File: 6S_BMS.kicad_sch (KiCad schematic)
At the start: 46 parts, among them J1 JST_EH_B8B-EH-A, J2 BM06B-GHS-TBT, J3 Conn_ARM_SWD_TagConnect_TC203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, J5 Conn_01x04_Pin, J6 Conn_01x04_Pin, SW1 SW_SPST, U1 BQ76925RGER, U2 STM32L431KCUx, U5 TLV75533PDBV

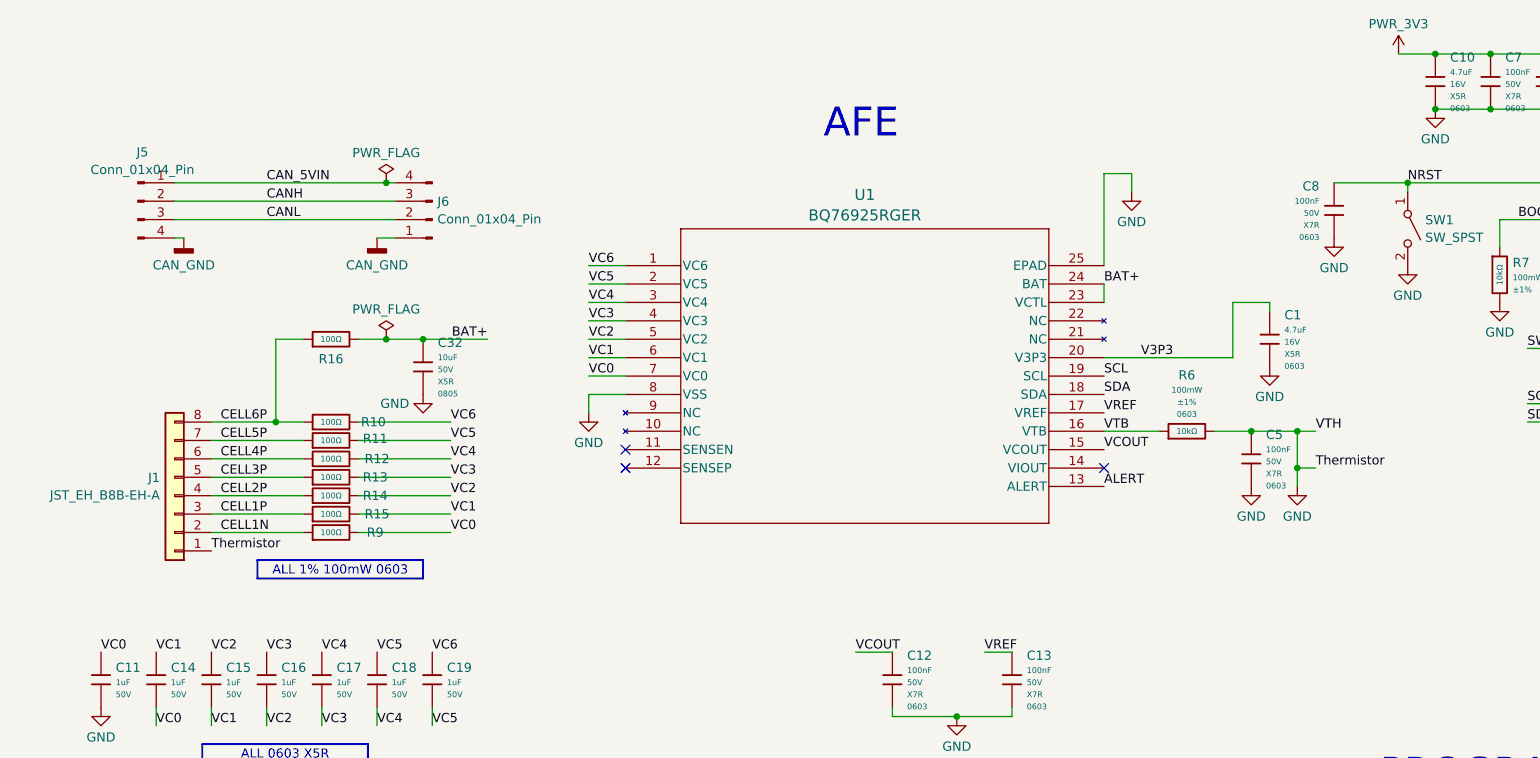
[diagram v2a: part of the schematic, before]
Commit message: Updated thermistor & layout
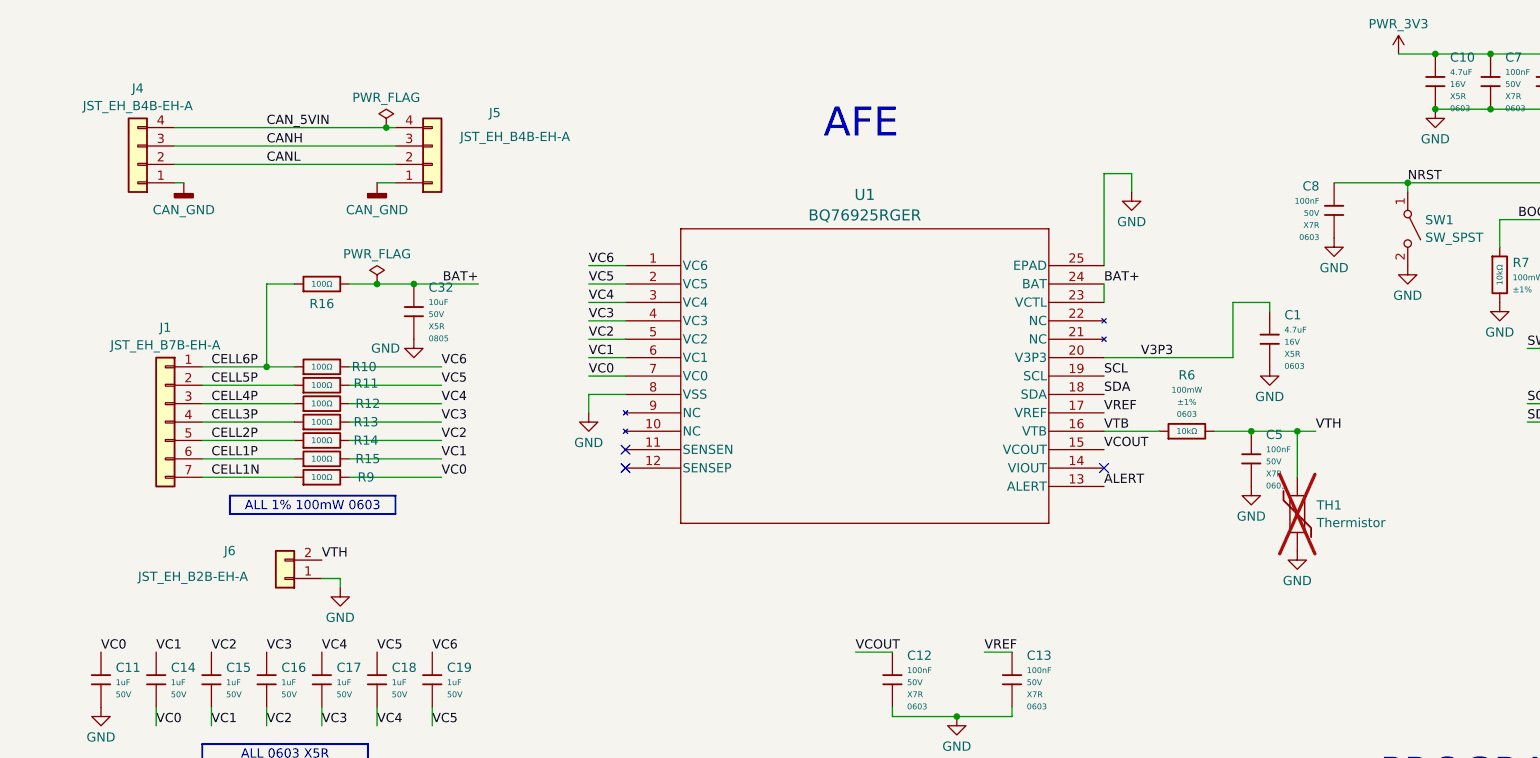
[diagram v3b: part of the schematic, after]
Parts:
- removed J1: JST_EH_B8B-EH-A, Connector_JST:JST_EH_B8B-EH-A_1x08_P2.50mm_Vertical, symbol Connector_Generic:Conn_01x08
- removed J5, J6: Conn_01x04_Pin, symbol Connector:Conn_01x04_Pin
- added J1: JST_EH_B7B-EH-A, Connector_JST:JST_EH_B7B-EH-A_1x07_P2.50mm_Vertical, symbol Connector_Generic:Conn_01x07
- added J4, J5: JST_EH_B4B-EH-A, Connector_JST:JST_EH_B4B-EH-A_1x04_P2.50mm_Vertical, symbol Connector_Generic:Conn_01x04
- added J6: JST_EH_B2B-EH-A, Connector_JST:JST_EH_B2B-EH-A_1x02_P2.50mm_Vertical, symbol Connector_Generic:Conn_01x02
- added TH1: Thermistor, symbol Device:Thermistor
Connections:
- net CANH: now also J4.3 (Pin_3), J5.3 (Pin_3)
- net CANL: now also J4.2 (Pin_2), J5.2 (Pin_2)
- net CAN_5VIN: now also J4.4 (Pin_4), J5.4 (Pin_4)
- net CAN_GND: now also J4.1 (Pin_1), J5.1 (Pin_1)
- net CELL1N: now also J1.7 (Pin_7)
- net CELL1P: now also J1.6 (Pin_6)
- net CELL2P: now also J1.5 (Pin_5)
- net CELL3P: now also J1.4 (Pin_4)
- net CELL4P: now also J1.3 (Pin_3)
- net CELL5P: now also J1.2 (Pin_2)
- net CELL6P: now also J1.1 (Pin_1)
- net GND: now also J6.1 (Pin_1), TH1.2; no longer C5.1, R6.2, U2.8 (PA2)
- new net VTH: C5.1, J6.2 (Pin_2), R6.2, TH1.1, U2.8 (PA2)
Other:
- moved on the sheet: C32, R10, R11, R12, R13, R14, R15, R16, R9
